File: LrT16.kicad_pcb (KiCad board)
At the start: 4 copper layers, 100 x 100 mm, 251 parts, among them J1 USB_C_Receptacle_USB2.0, J2 Conn_02x05_Odd_Even, Q1 2N7002, Q2 2N7002, SW1 EC11_SMD, SW10 EC11_SMD, SW11 EC11_SMD, SW12 EC11_SMD, SW13 EC11_SMD, SW14 EC11_SMD, SW15 EC11_SMD, SW16 EC11_SMD, SW17 SW_Push, SW18 SW_Push, SW2 EC11_SMD, SW20 SW_SPST, SW3 EC11_SMD, SW4 EC11_SMD, SW5 EC11_SMD, SW6 EC11_SMD, SW7 EC11_SMD, SW8 EC11_SMD, SW9 EC11_SMD, U1 STM32F072C8Tx, U2 SPX3819M5-L3-3TR

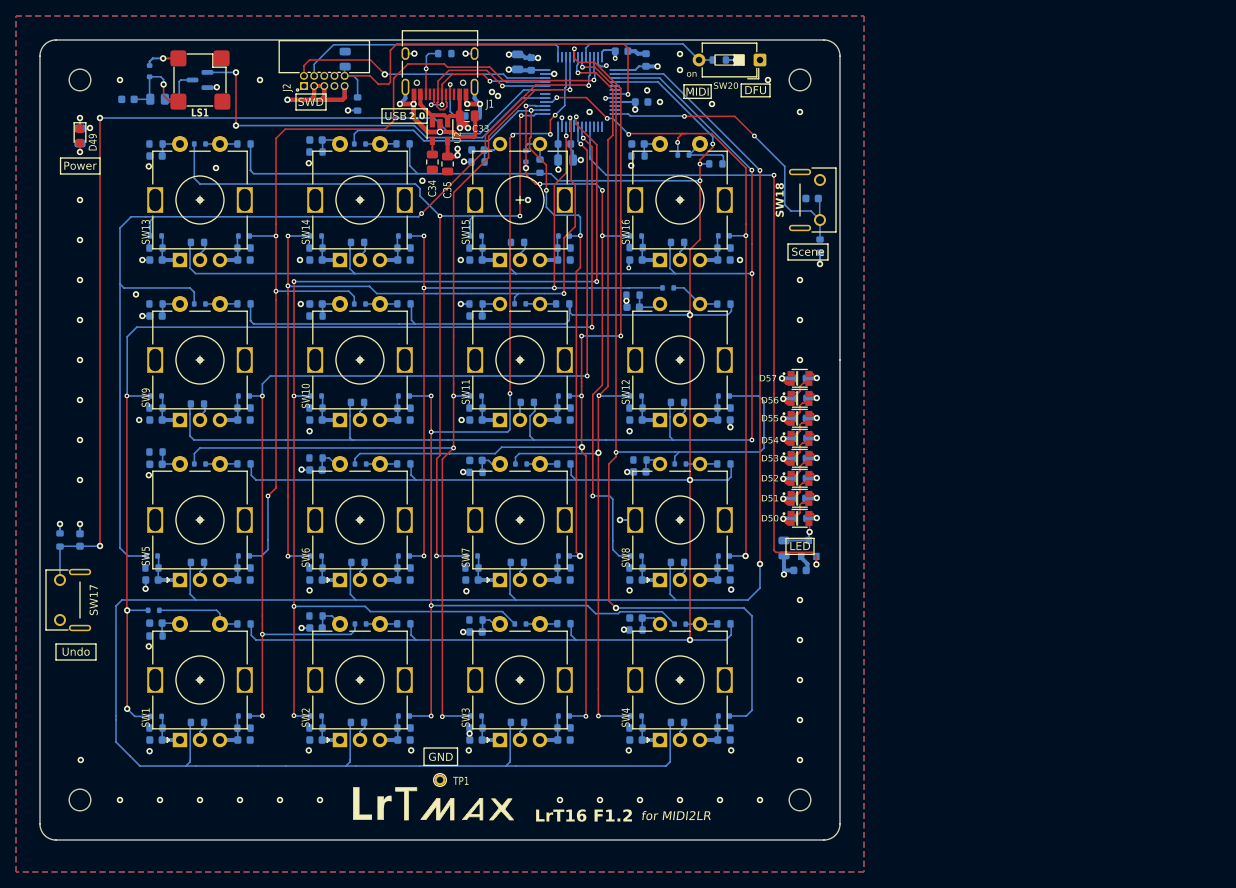
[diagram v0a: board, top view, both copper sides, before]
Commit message: Mod. switch debouncer
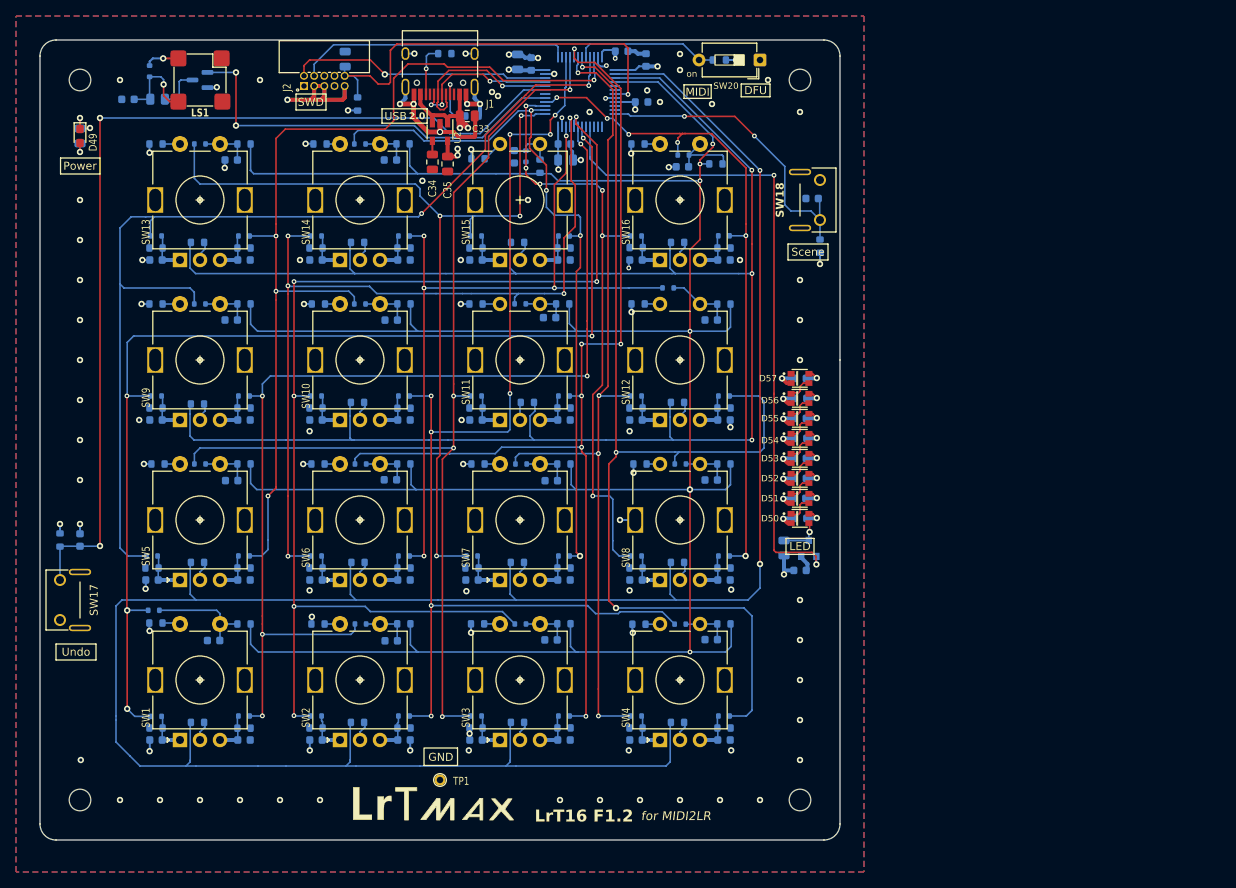
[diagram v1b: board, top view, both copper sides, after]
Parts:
- moved C65 9.88 mm to (183.9, 135.0)
- moved C59 9.78 mm to (183.9, 175.0)
- moved C61 9.74 mm to (163.9, 155.1)
- moved C72 9.67 mm to (124.0, 155.1)
- moved C67 9.63 mm to (143.8, 115.0)
- moved C63 9.61 mm to (143.9, 135.0)
- moved C71 9.54 mm to (143.9, 175.1)
- moved C58 9.42 mm to (163.9, 175.0)
- moved C66 9.41 mm to (123.9, 115.0)
- moved C73 9.41 mm to (123.9, 135.0)
- moved C60 9.38 mm to (143.8, 155.0)
- moved C64 9.20 mm to (163.7, 134.7)
- moved C62 8.98 mm to (183.9, 155.0)
- moved C70 7.53 mm to (121.7, 175.1)
- moved C69 6.24 mm to (180.3, 115.8)
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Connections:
- C58 pad 1: Net-(C58-Pad1) -> Net-(D7-A)
- C59 pad 1: Net-(C59-Pad1) -> Net-(D10-A)
- C60 pad 1: Net-(C60-Pad1) -> Net-(D16-A)
- C61 pad 1: Net-(C61-Pad1) -> Net-(D19-A)
- C62 pad 1: Net-(C62-Pad1) -> Net-(D22-A)
- C63 pad 1: Net-(C63-Pad1) -> Net-(D28-A)
- C64 pad 1: Net-(C64-Pad1) -> Net-(D31-A)
- C65 pad 1: Net-(C65-Pad1) -> Net-(D34-A)
- C66 pad 1: Net-(C66-Pad1) -> Net-(D37-A)
- C67 pad 1: Net-(C67-Pad1) -> Net-(D40-A)
- C68 pad 1: Net-(C68-Pad1) -> Net-(D43-A)
- C69 pad 1: Net-(C69-Pad1) -> Net-(D46-A)
- C70 pad 1: Net-(C70-Pad1) -> Net-(D1-A)
- C71 pad 1: Net-(C71-Pad1) -> Net-(D4-A)
- C72 pad 1: Net-(C72-Pad1) -> Net-(D13-A)
- C73 pad 1: Net-(C73-Pad1) -> Net-(D25-A)
- R40 pad 2: Net-(C70-Pad1) -> Net-(R40-Pad2)
- R41 pad 2: Net-(C71-Pad1) -> Net-(R41-Pad2)
- R42 pad 2: Net-(C58-Pad1) -> Net-(R42-Pad2)
- R43 pad 2: Net-(C59-Pad1) -> Net-(R43-Pad2)
- R44 pad 2: Net-(C72-Pad1) -> Net-(R44-Pad2)
- R45 pad 2: Net-(C60-Pad1) -> Net-(R45-Pad2)
- R46 pad 2: Net-(C61-Pad1) -> Net-(R46-Pad2)
- R47 pad 2: Net-(C62-Pad1) -> Net-(R47-Pad2)
- R48 pad 2: Net-(C73-Pad1) -> Net-(R48-Pad2)
- R49 pad 2: Net-(C63-Pad1) -> Net-(R49-Pad2)
- R50 pad 2: Net-(C64-Pad1) -> Net-(R50-Pad2)
- R51 pad 2: Net-(C65-Pad1) -> Net-(R51-Pad2)
- R52 pad 2: Net-(C66-Pad1) -> Net-(R52-Pad2)
- R53 pad 2: Net-(C67-Pad1) -> Net-(R53-Pad2)
- R54 pad 2: Net-(C68-Pad1) -> Net-(R54-Pad2)
- R55 pad 2: Net-(C69-Pad1) -> Net-(R55-Pad2)
- SW1 pad S2: Net-(C70-Pad1) -> Net-(R40-Pad2)
- SW10 pad S2: Net-(C63-Pad1) -> Net-(R49-Pad2)
- SW11 pad S2: Net-(C64-Pad1) -> Net-(R50-Pad2)
- SW12 pad S2: Net-(C65-Pad1) -> Net-(R51-Pad2)
- SW13 pad S2: Net-(C66-Pad1) -> Net-(R52-Pad2)
- SW14 pad S2: Net-(C67-Pad1) -> Net-(R53-Pad2)
- SW15 pad S2: Net-(C68-Pad1) -> Net-(R54-Pad2)
- SW16 pad S2: Net-(C69-Pad1) -> Net-(R55-Pad2)
- SW2 pad S2: Net-(C71-Pad1) -> Net-(R41-Pad2)
- SW3 pad S2: Net-(C58-Pad1) -> Net-(R42-Pad2)
- SW4 pad S2: Net-(C59-Pad1) -> Net-(R43-Pad2)
- SW5 pad S2: Net-(C72-Pad1) -> Net-(R44-Pad2)
- SW6 pad S2: Net-(C60-Pad1) -> Net-(R45-Pad2)
- SW7 pad S2: Net-(C61-Pad1) -> Net-(R46-Pad2)
- SW8 pad S2: Net-(C62-Pad1) -> Net-(R47-Pad2)
- SW9 pad S2: Net-(C73-Pad1) -> Net-(R48-Pad2)
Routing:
- net /L2: track 349.9 -> 365.9 mm
- net GND: track 112.6 -> 126.8 mm
- net Net-(C65-Pad1): track 4.26 -> 0.00 mm
- net Net-(C71-Pad1): track 4.11 -> 0.00 mm
- net Net-(C59-Pad1): track 4.06 -> 0.00 mm
- net Net-(C60-Pad1): track 4.01 -> 0.00 mm
- net Net-(C67-Pad1): track 3.95 -> 0.00 mm
- net Net-(C68-Pad1): track 3.94 -> 0.00 mm
- net Net-(C61-Pad1): track 3.93 -> 0.00 mm
- net Net-(C70-Pad1): track 3.91 -> 0.00 mm
- net Net-(C58-Pad1): track 3.90 -> 0.00 mm
- net Net-(C72-Pad1): track 3.80 -> 0.00 mm
- net Net-(C63-Pad1): track 3.75 -> 0.00 mm
- net Net-(C73-Pad1): track 3.70 -> 0.00 mm
- net Net-(C66-Pad1): track 3.70 -> 0.00 mm
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
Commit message: clean up
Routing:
- net /M9: track 119.3 -> 120.3 mm

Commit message: clean up2
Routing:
- net GND: track 126.8 -> 132.6 mm, vias 125 -> 138
- net /M4: track 131.3 -> 129.2 mm
- net /M6: track 105.7 -> 104.0 mm
- net /M14: track 75.9 -> 77.3 mm
- net Net-(R54-Pad2): track 2.82 -> 3.59 mm
- net /M7: track 135.6 -> 134.8 mm
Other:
- board text added: "PARTS SIDE LAYER"
- board text added: "PARTS SIDE RESIST"
- board text added: "PARTS SIDE SILK"
- board text added: "SOLDER SIDE LAYER"
- board text added: "SOLDER SIDE RESIST"
- board text added: "SOLDER SIDE SILK"
- board text removed: "PARTS LAYER"
- board text removed: "PARTS RESIST"
- board text removed: "PARTS SILK"
- board text removed: "SOLDER LAYER"
- board text removed: "SOLDER RESIST"
- board text removed: "SOLDER SILK"

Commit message: clean up 3
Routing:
- net GND: vias 138 -> 148
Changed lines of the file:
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@@
 		(tags "resistor")
 		(property "Reference" "R85"
-			(at 2.71 0.006923 0)
+			(at 3.26 0.006923 0)
 			(layer "B.SilkS")
 			(effects
@@
 		(tags "capacitor")
 		(property "Reference" "C65"
-			(at 2.661732 -0.017834 0)
+			(at 3.161732 -0.017834 0)
 			(layer "B.SilkS")
 			(effects
@@
 	)
 	(via
-		(at 127.5 105)
+		(at 127 105)
 		(size 0.8)
 		(drill 0.4)
@@
 	)
 	(via
+		(at 162 175)
+		(size 0.8)
+		(drill 0.4)
+		(layers "F.Cu" "B.Cu")
+		(free yes)
+		(net 2)
+	)
+	(via
 		(at 142 175.25)
 		(size 0.8)
@@
 	)
 	(via
+		(at 141.75 115)
+		(size 0.8)
+		(drill 0.4)
+		(layers "F.Cu" "B.Cu")
+		(free yes)
+		(net 2)
+	)
+	(via
 		(at 165.5 123)
 		(size 0.8)
@@
 	)
 	(via
+		(at 126.25 168.75)
+		(size 0.8)
+		(drill 0.4)
+		(layers "F.Cu" "B.Cu")
+		(free yes)
+		(net 2)
+	)
+	(via
 		(at 162.25 102.25)
 		(size 0.8)
@@
 	)
 	(via
+		(at 105 185)
+		(size 0.8)
+		(drill 0.4)
+		(layers "F.Cu" "B.Cu")
+		(free yes)
+		(net 2)
+	)
+	(via
 		(at 105 150)
 		(size 0.8)
@@
 	)
 	(via
+		(at 166.322189 128.559129)
+		(size 0.6)
+		(drill 0.3)
+		(layers "F.Cu" "B.Cu")
+		(free yes)
+		(net 2)
+	)
+	(via
 		(at 156.5 106.5)
 		(size 0.8)
@@
 	)
 	(via
+		(at 182.25 135)
+		(size 0.8)
+		(drill 0.4)
+		(layers "F.Cu" "B.Cu")
+		(free yes)
+		(net 2)
+	)
+	(via
 		(at 180 195)
 		(size 0.8)
@@
 	)
 	(via
+		(at 182.25 155)
+		(size 0.8)
+		(drill 0.4)
+		(layers "F.Cu" "B.Cu")
+		(free yes)
+		(net 2)
+	)
+	(via
 		(at 113.7 188.9)
 		(size 0.8)
@@
 	)
 	(via
+		(at 105 180)
+		(size 0.8)
+		(drill 0.4)
+		(layers "F.Cu" "B.Cu")
+		(free yes)
+		(net 2)
+	)
+	(via
 		(at 170.8 103.2)
 		(size 0.6)
@@
 	)
 	(via
+		(at 127.25 126)
+		(size 0.8)
+		(drill 0.4)
+		(layers "F.Cu" "B.Cu")
+		(free yes)
+		(net 2)
+	)
+	(via
 		(at 122.1 105.9)
 		(size 0.8)
@@
 	)
 	(via
+		(at 122 155)
+		(size 0.8)
+		(drill 0.4)
+		(layers "F.Cu" "B.Cu")
+		(free yes)
+		(net 2)
+	)
+	(via
 		(at 132.5 127.5)
 		(size 0.8)
@@
 		(polygon
 			(pts
+				(xy 160.5 117) (xy 160.5 117.75) (xy 164 117.75) (xy 164 117)
+			)
+		)
+	)
+	(zone
+		(net 0)
+		(net_name "")
+		(layer "B.Cu")
+		(hatch edge 0.5)
+		(connect_pads
+			(clearance 0)
+		)
+		(min_thickness 0.25)
+		(filled_areas_thickness no)
+		(keepout
+			(tracks allowed)
+			(vias allowed)
+			(pads allowed)
+			(copperpour not_allowed)
+			(footprints allowed)
+		)
+		(placement
+			(enabled no)
+			(sheetname "")
+		)
+		(fill
+			(thermal_gap 0.5)
+			(thermal_bridge_width 0.5)
+		)
+		(polygon
+			(pts
 				(xy 124.3674 123.766437) (xy 123.7674 126) (xy 121.1674 126.020598) (xy 121.1674 124.566437) (xy 118.1674 124.566437)
 				(xy 118.1674 125.966437) (xy 116.3674 125.966437) (xy 115.5674 123.766437) (xy 114 123.8) (xy 114 128.8)
@@
 				(xy 124.6 143.8) (xy 123.728718 146.190769) (xy 121.128718 146.204334) (xy 121.128718 144.790769)
 				(xy 118.128718 144.790769) (xy 118.128718 146.190769) (xy 116.4 146.2) (xy 115.8 143.8) (xy 113.682053 143.8)
-				(xy 113.692183 149.829624) (xy 116.492183 149.829624) (xy 125.928718 149.829624) (xy 126 143.8)
+				(xy 113.691007 148.5) (xy 114.392183 149.829624) (xy 116.492183 149.829624) (xy 125.928718 149.829624)
+				(xy 126 143.8)
 			)
 		)
@@
 		(polygon
 			(pts
+				(xy 164.5 119.2) (xy 164.5 120.8) (xy 164 120.8) (xy 164 119.2)
+			)
+		)
+	)
+	(zone
+		(net 0)
+		(net_name "")
+		(layer "B.Cu")
+		(hatch edge 0.5)
+		(connect_pads
+			(clearance 0)
+		)
+		(min_thickness 0.25)
+		(filled_areas_thickness no)
+		(keepout
+			(tracks allowed)
+			(vias allowed)
+			(pads allowed)
+			(copperpour not_allowed)
+			(footprints allowed)
+		)
+		(placement
+			(enabled no)
+			(sheetname "")
+		)
+		(fill
+			(thermal_gap 0.5)
+			(thermal_bridge_width 0.5)
+		)
+		(polygon
+			(pts
 				(xy 172.6 134.8) (xy 172.6 136.5) (xy 172.4 136.5) (xy 172.4 134.8)
 			)
@@
 		(polygon
 			(pts
-				(xy 174.5 134) (xy 186.75 134) (xy 186.75 131.5) (xy 174.5 131.5)
+				(xy 174.5 134) (xy 186.75 134) (xy 186.75 129.5) (xy 174.5 131.5)
 			)
 		)
